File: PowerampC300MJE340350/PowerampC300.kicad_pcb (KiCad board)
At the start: 2 copper layers, 240 x 63 mm, 109 parts, among them J1 Conn_01x02, J2 Conn_01x02, J3 Conn_01x02, J4 Conn_01x01, J5 Conn_01x01, J6 Conn_01x01, J7 Conn_01x01, J8 Conn_01x02, J9 Conn_Coaxial, Q1 2N5551, Q10 MJE15033, Q11 MJE15032, Q12 MJE15032, Q13 2N5551, Q14 2N5401, Q15 MJE15032, Q16 MJE15033, Q17 MJL3281A, Q18 MJL1302A, Q19 MJL3281A, Q2 2N5551, Q20 MJL1302A, Q21 MJL3281A, Q22 MJL1302A, Q23 MJL3281A, Q24 MJL1302A, Q3 2N5401, Q4 2N5401, Q5 2N5551, Q6 2N5551, Q7 2N5551, Q8 2N5401, Q9 2N5401

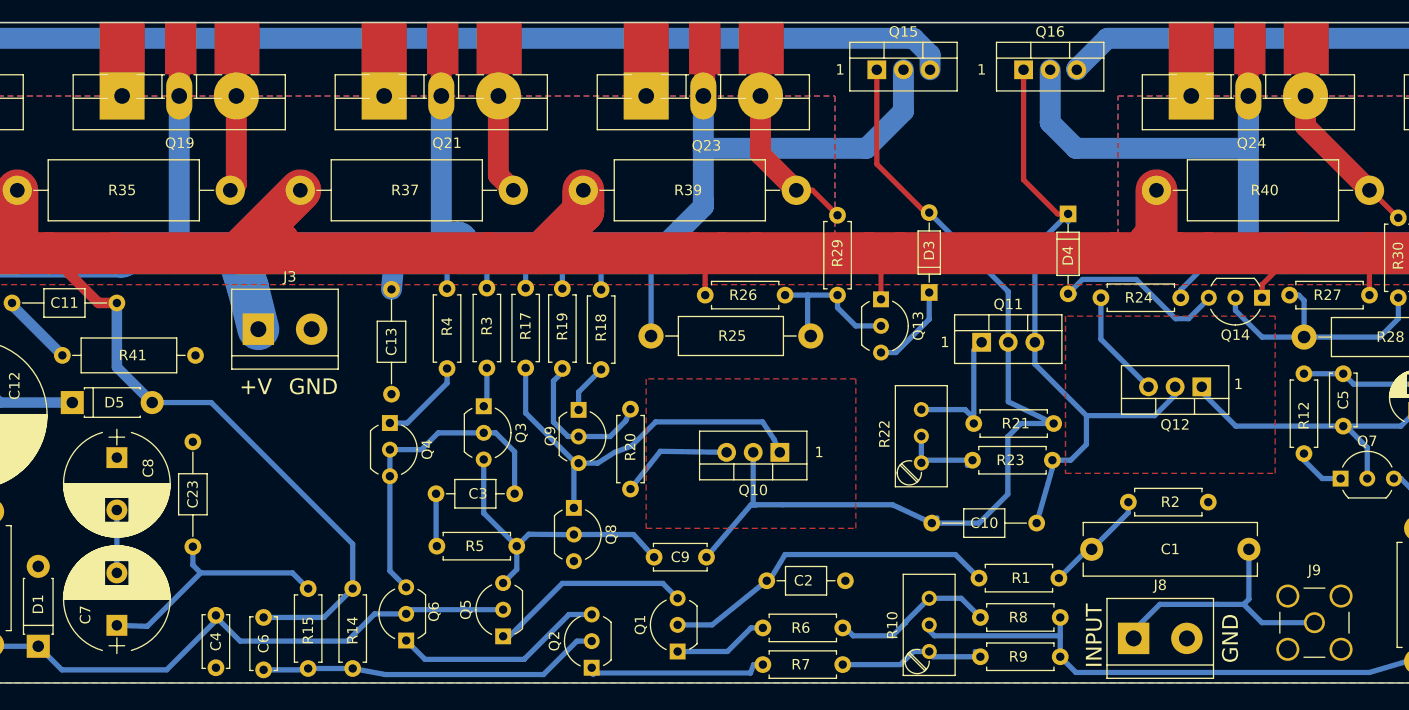
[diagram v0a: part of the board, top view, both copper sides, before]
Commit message: Some more layout changed and XlrtoBal fix
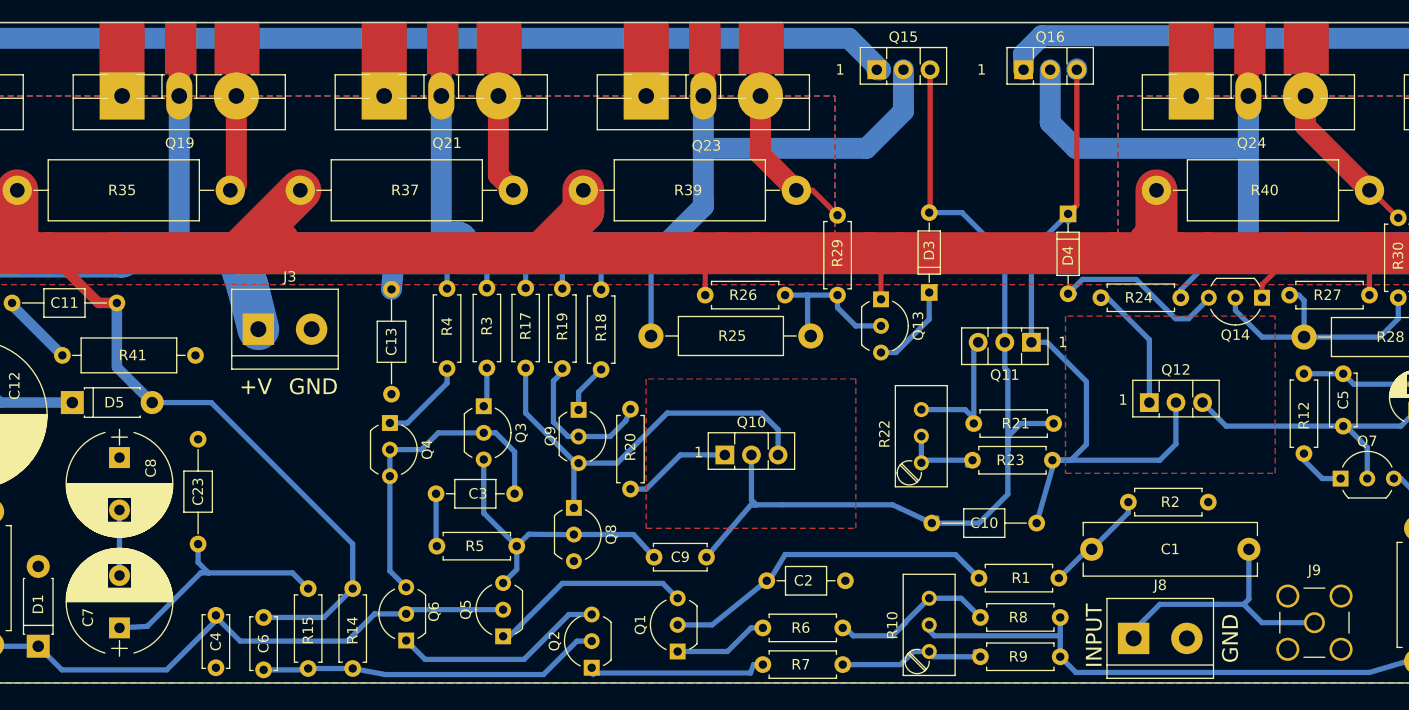
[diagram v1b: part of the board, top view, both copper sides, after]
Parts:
- Q10, Q16: value MJE15033 -> MJE350; footprint TO_SOT_Packages_THT:TO-220-3_Vertical -> TO_SOT_Packages_THT:TO-126_Vertical
- Q11, Q12, Q15: value MJE15032 -> MJE340; footprint TO_SOT_Packages_THT:TO-220-3_Vertical -> TO_SOT_Packages_THT:TO-126_Vertical
- moved Q10 5.26 mm to (122.5, 84.2), turned to 0 degrees
- moved Q12 5.22 mm to (163.0, 79.2), turned to 0 degrees
- moved Q11 4.75 mm to (151.8, 73.5), turned to 180 degrees
- moved C23 0.56 mm to (72.2, 82.8)
- moved C7 0.35 mm to (64.8, 100.8)
- moved C8 0.25 mm to (64.8, 84.5)
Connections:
- Q11 pad 1: Net-(Q11-Pad1) -> Net-(C10-Pad1)
- Q11 pad 3: Net-(C10-Pad1) -> Net-(Q11-Pad3)
- Q12 pad 1: Net-(C22-Pad1) -> Net-(Q12-Pad1)
- Q12 pad 3: Net-(Q12-Pad3) -> Net-(C22-Pad1)
- Q15 pad 1: Net-(C10-Pad2) -> Net-(Q15-Pad1)
- Q15 pad 3: Net-(Q15-Pad3) -> Net-(C10-Pad2)
- Q16 pad 1: Net-(C10-Pad1) -> Net-(Q16-Pad1)
- Q16 pad 3: Net-(Q16-Pad3) -> Net-(C10-Pad1)
- Q17 pad 1: Net-(Q15-Pad3) -> Net-(Q15-Pad1)
- Q18 pad 1: Net-(Q16-Pad3) -> Net-(Q16-Pad1)
- Q19 pad 1: Net-(Q15-Pad3) -> Net-(Q15-Pad1)
- Q20 pad 1: Net-(Q16-Pad3) -> Net-(Q16-Pad1)
- Q21 pad 1: Net-(Q15-Pad3) -> Net-(Q15-Pad1)
- Q22 pad 1: Net-(Q16-Pad3) -> Net-(Q16-Pad1)
- Q23 pad 1: Net-(Q15-Pad3) -> Net-(Q15-Pad1)
- Q24 pad 1: Net-(Q16-Pad3) -> Net-(Q16-Pad1)
- Q8 pad 1: Net-(Q10-Pad1) -> Net-(Q10-Pad3)
- Q9 pad 3: Net-(Q10-Pad1) -> Net-(Q10-Pad3)
- R17 pad 1: Net-(Q10-Pad1) -> Net-(Q10-Pad3)
- R20 pad 1: Net-(Q10-Pad3) -> Net-(Q10-Pad1)
- R21 pad 1: Net-(Q11-Pad1) -> Net-(Q11-Pad3)
- R22 pad 3: Net-(Q11-Pad1) -> Net-(Q11-Pad3)
- R24 pad 2: Net-(Q12-Pad3) -> Net-(Q12-Pad1)
- R31 pad 2: Net-(Q15-Pad3) -> Net-(Q15-Pad1)
- R32 pad 1: Net-(Q16-Pad3) -> Net-(Q16-Pad1)
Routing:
- net Net-(Q16-Pad1): track 0.00 -> 160.9 mm
- net Net-(Q15-Pad3): track 159.5 -> 0.00 mm
- net Net-(Q15-Pad1): track 0.00 -> 154.3 mm
- net Net-(Q16-Pad3): track 153.8 -> 0.00 mm
- net Net-(Q10-Pad3): track 10.9 -> 40.3 mm
- net Net-(Q10-Pad1): track 38.4 -> 10.3 mm
- net Net-(Q11-Pad3): track 0.00 -> 14.3 mm
- net Net-(Q11-Pad1): track 13.9 -> 0.00 mm
- net Net-(Q12-Pad1): track 0.00 -> 12.3 mm
- net Net-(Q12-Pad3): track 10.5 -> 0.00 mm
- net Net-(C10-Pad1): track 63.3 -> 68.1 mm
- net Net-(C22-Pad1): track 39.6 -> 38.6 mm
- net Net-(C10-Pad2): track 91.7 -> 91.2 mm

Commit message: JLCPCB order 2020-09-21
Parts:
- moved C11 177.3 mm to (230.3, 92.4), turned to 90 degrees
- moved R41 155.0 mm to (226.8, 82.4), turned to 90 degrees
- moved C19 53.2 mm to (253.0, 94.2), turned to 90 degrees
- moved L1 51.6 mm to (209.6, 82.0), turned to 90 degrees
- moved C14 47.9 mm to (257.4, 78.8)
- moved J3 40.5 mm to (41.8, 90.5), turned to 180 degrees
- moved D9 37.7 mm to (57.6, 101.4), turned to 0 degrees
- moved D7 31.0 mm to (46.7, 101.5), turned to 0 degrees
- moved J2 26.8 mm to (242.0, 95.6), turned to 180 degrees
- moved J1 24.7 mm to (220.8, 100.4), turned to 180 degrees
- moved C18 22.4 mm to (242.0, 78.8), turned to 90 degrees
- moved D1 21.1 mm to (75.8, 93.0), turned to 0 degrees
- moved R13 20.7 mm to (71.2, 93.4)
- moved C7 20.5 mm to (79.8, 86.8)
- moved C8 20.5 mm to (79.6, 70.4)
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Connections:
- C11 pad 1: Net-(C11-Pad1) -> GND
- C6 pad 2: Net-(C11-Pad2) -> Net-(C6-Pad2)
- D5 pad 2: Net-(C11-Pad2) -> Net-(C6-Pad2)
- D6 pad 1: Net-(C11-Pad2) -> Net-(C6-Pad2)
- L1 pad 2: Net-(C11-Pad2) -> Net-(C6-Pad2)
- Q13 pad 1: Net-(C11-Pad2) -> Net-(C6-Pad2)
- Q14 pad 1: Net-(C11-Pad2) -> Net-(C6-Pad2)
- R14 pad 1: Net-(C11-Pad2) -> Net-(C6-Pad2)
- R26 pad 2: Net-(C11-Pad2) -> Net-(C6-Pad2)
- R27 pad 1: Net-(C11-Pad2) -> Net-(C6-Pad2)
- R31 pad 1: Net-(C11-Pad2) -> Net-(C6-Pad2)
- R32 pad 2: Net-(C11-Pad2) -> Net-(C6-Pad2)
- R33 pad 1: Net-(C11-Pad2) -> Net-(C6-Pad2)
- R34 pad 2: Net-(C11-Pad2) -> Net-(C6-Pad2)
- R35 pad 1: Net-(C11-Pad2) -> Net-(C6-Pad2)
- R36 pad 2: Net-(C11-Pad2) -> Net-(C6-Pad2)
- R37 pad 1: Net-(C11-Pad2) -> Net-(C6-Pad2)
- R38 pad 2: Net-(C11-Pad2) -> Net-(C6-Pad2)
- R39 pad 1: Net-(C11-Pad2) -> Net-(C6-Pad2)
- R40 pad 2: Net-(C11-Pad2) -> Net-(C6-Pad2)
- R41 pad 1: GND -> Net-(C11-Pad2)
- R41 pad 2: Net-(C11-Pad1) -> Net-(C6-Pad2)
- R42 pad 1: Net-(C11-Pad2) -> Net-(C6-Pad2)
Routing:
- net Net-(C6-Pad2): track 0.00 -> 450.1 mm, vias 0 -> 1
- net Net-(C11-Pad2): track 406.1 -> 3.54 mm
- net -48V: track 319.7 -> 298.7 mm
- net OUTPUT: track 40.7 -> 28.3 mm
- net Net-(C4-Pad2): track 56.0 -> 44.0 mm
- net Net-(D10-Pad2): track 3.78 -> 10.8 mm
- net Net-(C11-Pad1): track 6.99 -> 0.00 mm
- net +48V: track 301.1 -> 307.7 mm
- net Net-(C10-Pad1): track 68.1 -> 63.8 mm
- net Net-(R10-Pad2): track 52.0 -> 55.8 mm
- net INPUT: track 25.2 -> 22.0 mm
- net Net-(Q10-Pad3): track 40.3 -> 43.1 mm
- net Net-(C1-Pad1): track 10.2 -> 12.9 mm
- net Net-(R10-Pad3): track 15.8 -> 13.4 mm
- net Net-(C22-Pad1): track 38.6 -> 41.0 mm
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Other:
- board text added: "MODIFIED C300 AMPLIFIER BY DANIEL MARKS ORIGINAL BY MICHAEL CHUA (AMPSLAB) CC-BY-SA 4.0 V2"
- board text removed: "C300 AMPLIFIER PCB BY DANIEL MARKS C300 DESIGNED BY MICHAEL CHUA (AMPSLAB) CC-BY-SA 4.0 V2"

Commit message: Working design 2020-10-12
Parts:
- removed Q9: 2N5401, TO_SOT_Packages_THT:TO-92_Inline_Wide
- removed R18: 330R, Resistors_THT:R_Axial_DIN0207_L6.3mm_D2.5mm_P7.62mm_Horizontal
- removed R20: 27R, Resistors_THT:R_Axial_DIN0207_L6.3mm_D2.5mm_P7.62mm_Horizontal
- added R43: 10k, Resistors_THT:R_Axial_DIN0309_L9.0mm_D3.2mm_P12.70mm_Horizontal, F.Cu at (193.5, 101.8)
- R19: value 10R -> 33R; footprint Resistors_THT:R_Axial_DIN0207_L6.3mm_D2.5mm_P7.62mm_Horizontal -> Resistors_THT:R_Axial_DIN0309_L9.0mm_D3.2mm_P12.70mm_Horizontal
- R23: value 150R -> 100R
- moved R19 8.32 mm to (110.8, 83.4)
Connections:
- R19 pad 1: Net-(Q9-Pad2) -> Net-(Q10-Pad1)
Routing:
- net Net-(C6-Pad2): track 450.1 -> 486.7 mm
- net Net-(Q9-Pad2): track 15.6 -> 0.00 mm
- net +48V: track 307.7 -> 297.8 mm
- net Net-(Q9-Pad1): track 5.95 -> 0.00 mm
- net Net-(Q10-Pad3): track 43.1 -> 39.9 mm
- net Net-(Q10-Pad1): track 12.5 -> 15.3 mm

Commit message: Changed grounding and star layout
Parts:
- removed C20, C21: 0.1 uF, Capacitors_THT:C_Disc_D5.0mm_W2.5mm_P5.00mm
- added C24: SHORT, Capacitors_THT:C_Disc_D5.0mm_W2.5mm_P5.00mm, F.Cu at (134.5, 93.2)
- added C25: 0.1 uF, Capacitors_THT:C_Axial_L3.8mm_D2.6mm_P10.00mm_Horizontal, F.Cu at (121.9, 92.8)
- added JP1: Jumper_NO_Small, Pin_Headers:Pin_Header_Straight_1x02_Pitch2.54mm, F.Cu at (263.4, 93.2)
- added JP2: Jumper_NO_Small, Pin_Headers:Pin_Header_Straight_1x02_Pitch2.54mm, F.Cu at (28.7, 93.5)
- added R18: NC, Resistors_THT:R_Axial_DIN0207_L6.3mm_D2.5mm_P7.62mm_Horizontal, F.Cu at (111.8, 91.7)
- C3: value 220 pF -> 150 pF
- C9: value 100 pF -> 150 pF
- moved C8 25.0 mm to (76.4, 95.2), turned to 90 degrees
- moved D10 21.9 mm to (248.0, 103.0)
- moved D8 16.6 mm to (248.0, 100.0)
- moved J2 8.60 mm to (242.0, 87.0)
- moved C7 8.13 mm to (76.4, 79.4), turned to 270 degrees
- moved C23 7.41 mm to (65.6, 104.4)
- moved C16 6.89 mm to (40.5, 79.2), turned to 90 degrees
- moved D1 6.67 mm to (70.1, 96.5), turned to 270 degrees
- moved C12 6.48 mm to (55.6, 79.2), turned to 90 degrees
- moved C17 6.46 mm to (55.4, 94.4), turned to 90 degrees
- moved R13 6.39 mm to (65.5, 90.4)
- moved R2 6.25 mm to (161.0, 95.0)
- moved C9 4.81 mm to (111.0, 94.6)
- moved D5 3.72 mm to (69.7, 77.6)
- moved J3 3.51 mm to (42.0, 87.0)
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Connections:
- C9 pad 2: Net-(C10-Pad2) -> Net-(C24-Pad1)
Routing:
- net Net-(C24-Pad1): track 0.00 -> 31.3 mm
- net Net-(C4-Pad2): track 44.0 -> 58.0 mm
- net Net-(C23-Pad2): track 26.3 -> 39.3 mm
- net Net-(C10-Pad2): track 91.2 -> 83.3 mm
- net Net-(C9-Pad1): track 31.2 -> 26.3 mm
- net Net-(Q10-Pad3): track 39.9 -> 44.2 mm
- net -48V: track 298.7 -> 302.5 mm
- net Net-(C3-Pad2): track 30.9 -> 34.6 mm
- net Net-(J4-Pad1): track 5.58 -> 8.87 mm
- net Net-(C25-Pad1): track 0.00 -> 2.92 mm
- net Net-(C6-Pad2): track 486.7 -> 484.0 mm
- net INPUT: track 22.0 -> 24.2 mm
- net Net-(C3-Pad1): track 5.26 -> 3.64 mm
- net Net-(C2-Pad2): track 31.8 -> 30.3 mm
- net Net-(J6-Pad1): track 5.00 -> 6.54 mm
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
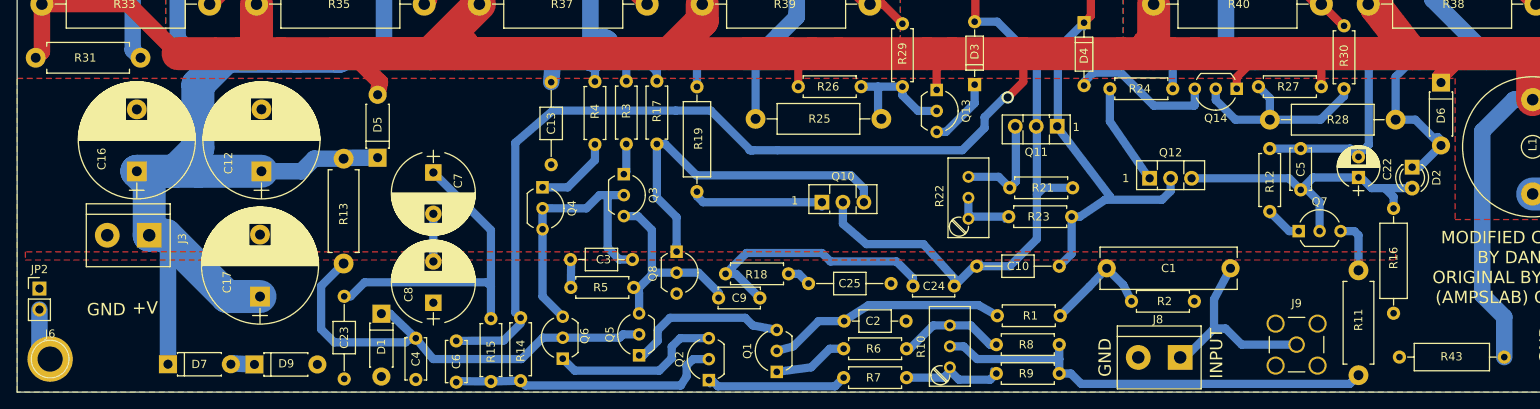
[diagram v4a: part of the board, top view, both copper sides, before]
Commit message: Sample feedback from output directly
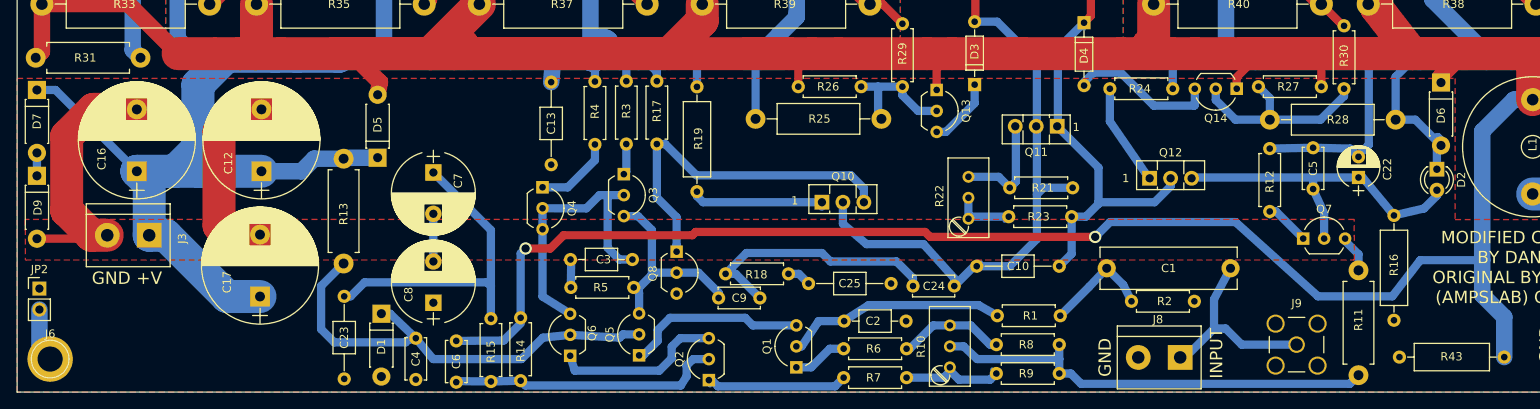
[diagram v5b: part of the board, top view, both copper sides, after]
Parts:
- moved D7 36.8 mm to (28.4, 69.4), turned to 270 degrees
- moved D9 34.9 mm to (28.4, 79.8), turned to 270 degrees
- moved D2 3.01 mm to (198.0, 79.0)
- moved Q1 2.44 mm to (120.4, 103.0)
- moved C5 1.50 mm to (183.0, 76.4)
- moved Q7 1.05 mm to (181.8, 87.4)
- moved Q6 0.97 mm to (93.0, 101.6)
- moved R16 0.85 mm to (192.8, 84.6)
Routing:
- net GND: track 0.75 -> 57.5 mm
- net Net-(C6-Pad2): track 484.0 -> 521.4 mm, vias 1 -> 2
- net -48V: track 302.5 -> 299.1 mm
- net Net-(Q7-Pad3): track 8.24 -> 5.47 mm
- net Net-(C22-Pad1): track 41.0 -> 43.5 mm
- net Net-(Q1-Pad1): track 9.07 -> 6.66 mm
- net Net-(Q1-Pad3): track 20.5 -> 22.8 mm
- net Net-(C2-Pad2): track 30.3 -> 28.2 mm
- net Net-(Q7-Pad1): track 5.13 -> 6.07 mm
